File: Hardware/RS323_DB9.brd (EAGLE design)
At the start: 21.6 x 30.5 mm, 16 parts, among them U2 XN04312

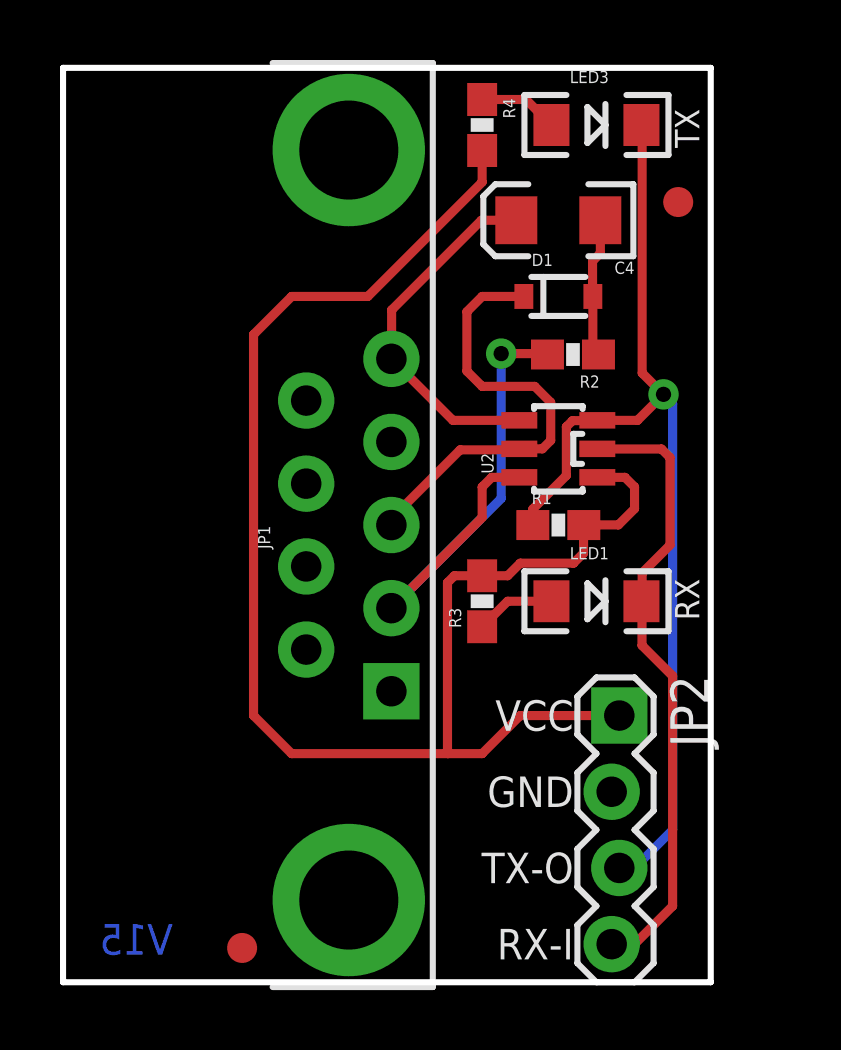
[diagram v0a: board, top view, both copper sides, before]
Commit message: Fixed headers, trace re route
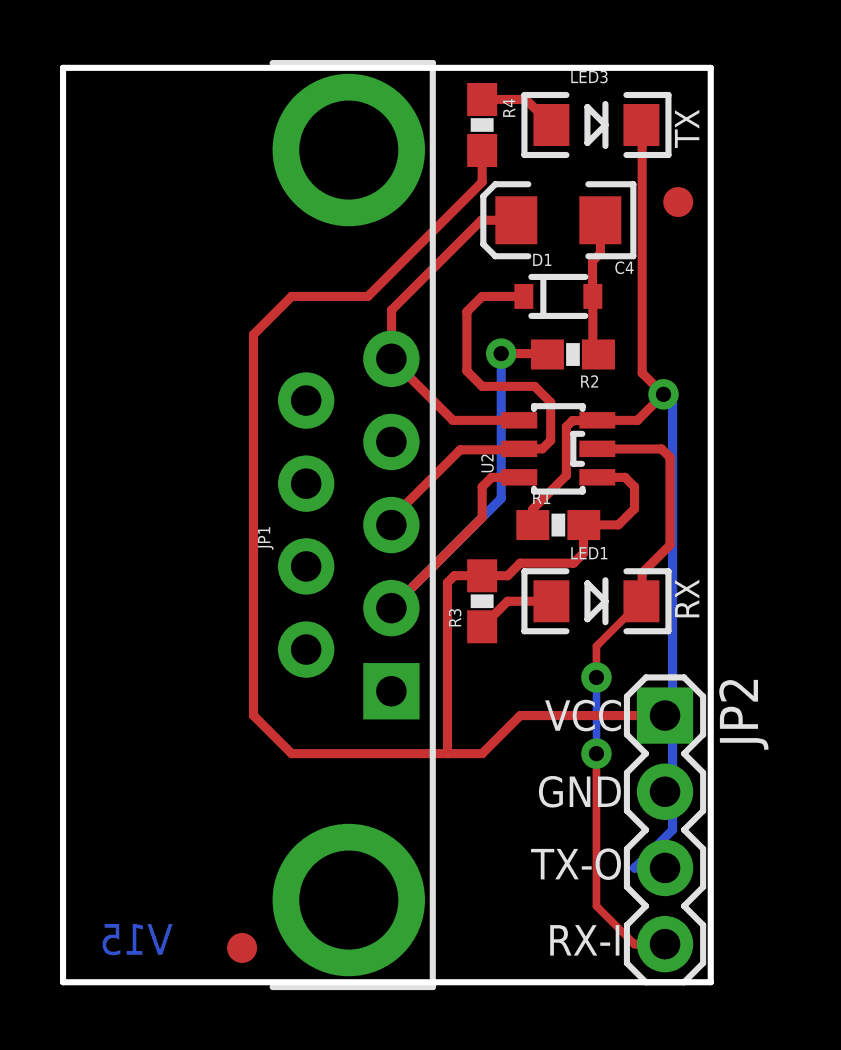
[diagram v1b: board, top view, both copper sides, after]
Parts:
- JP2: device SparkFun-Connectors:1X04_LOCK -> SparkFun-Connectors:1X04
- moved JP2 1.65 mm to (20.1, 8.89)
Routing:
- net VCC: track 52.7 -> 54.2 mm
- net TX: track 33.7 -> 34.2 mm
- net RX: track 21.1 -> 21.6 mm, vias 0 -> 2

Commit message: Fixed bad trace.
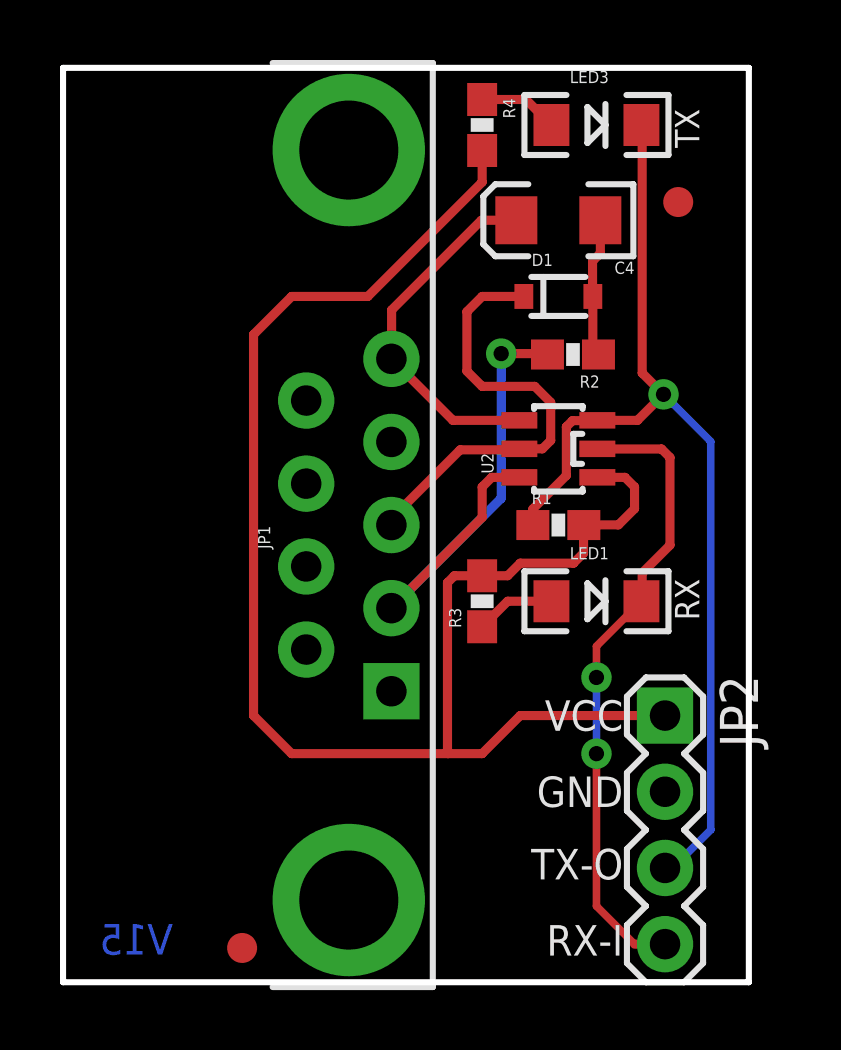
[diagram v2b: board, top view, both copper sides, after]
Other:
- board size 21.6 x 30.5 mm -> 22.9 x 30.5 mm
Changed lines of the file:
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@@
 <board>
 <plain>
-<wire x1="0" y1="0" x2="21.59" y2="0" width="0.2032" layer="20"/>
-<wire x1="21.59" y1="0" x2="21.59" y2="30.48" width="0.2032" layer="20"/>
-<wire x1="21.59" y1="30.48" x2="0" y2="30.48" width="0.2032" layer="20"/>
+<wire x1="0" y1="0" x2="22.86" y2="0" width="0.2032" layer="20"/>
+<wire x1="22.86" y1="0" x2="22.86" y2="30.48" width="0.2032" layer="20"/>
+<wire x1="22.86" y1="30.48" x2="0" y2="30.48" width="0.2032" layer="20"/>
 <wire x1="0" y1="30.48" x2="0" y2="0" width="0.2032" layer="20"/>
 <text x="18.669" y="1.905" size="1.016" layer="21" font="vector" ratio="15" rot="R180">RX-I</text>
@@
 <polygon width="0.2032" layer="16" isolate="0.3048">
 <vertex x="0" y="30.48"/>
-<vertex x="21.59" y="30.48"/>
-<vertex x="21.59" y="0"/>
+<vertex x="22.86" y="30.48"/>
+<vertex x="22.86" y="0"/>
 <vertex x="0" y="0"/>
 </polygon>
@@
 <wire x1="19.28" y1="28.472" x2="19.28" y2="28.575" width="0.3048" layer="1"/>
 <wire x1="19.304" y1="20.3073" x2="19.304" y2="28.448" width="0.3048" layer="1"/>
-<wire x1="20.066" y1="3.81" x2="19.05" y2="3.81" width="0.3048" layer="16"/>
-<wire x1="19.05" y1="3.81" x2="20.32" y2="5.08" width="0.3048" layer="16"/>
-<wire x1="20.32" y1="5.08" x2="20.32" y2="19.2913" width="0.3048" layer="16"/>
 <via x="20.0152" y="19.5961" extent="1-16" drill="0.508"/>
 <wire x1="20.32" y1="19.2913" x2="20.0152" y2="19.5961" width="0.3048" layer="16"/>
@@
 <wire x1="16.982440625" y1="18.7198" x2="17.7999" y2="18.7198" width="0.3048" layer="1"/>
 <wire x1="17.7999" y1="18.7198" x2="17.8101" y2="18.73" width="0.3048" layer="1"/>
+<wire x1="20.066" y1="3.81" x2="20.32" y2="3.81" width="0.254" layer="16"/>
+<wire x1="20.32" y1="3.81" x2="21.59" y2="5.08" width="0.254" layer="16"/>
+<wire x1="21.59" y1="5.08" x2="21.59" y2="18.0213" width="0.254" layer="16"/>
+<wire x1="21.59" y1="18.0213" x2="20.0152" y2="19.5961" width="0.254" layer="16"/>
 </signal>
 <signal name="N$4">

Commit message: fixed bad trace, added top ground plane.
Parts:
- FRAME1: value FRAME-LETTER -> (none)
- renumbered LED1 to D4, LED3 to D5
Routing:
- added copper zone on layer 1, net GND
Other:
- board text added: "N. Seidle"
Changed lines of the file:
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@@
 <layer number="27" name="tValues" color="7" fill="1" visible="no" active="yes"/>
 <layer number="28" name="bValues" color="7" fill="1" visible="no" active="yes"/>
-<layer number="29" name="tStop" color="7" fill="3" visible="no" active="yes"/>
+<layer number="29" name="tStop" color="7" fill="3" visible="yes" active="yes"/>
 <layer number="30" name="bStop" color="7" fill="6" visible="no" active="yes"/>
-<layer number="31" name="tCream" color="7" fill="4" visible="no" active="yes"/>
+<layer number="31" name="tCream" color="7" fill="4" visible="yes" active="yes"/>
 <layer number="32" name="bCream" color="7" fill="5" visible="no" active="yes"/>
 <layer number="33" name="tFinish" color="6" fill="3" visible="no" active="yes"/>
@@
 <layer number="39" name="tKeepout" color="4" fill="11" visible="no" active="yes"/>
 <layer number="40" name="bKeepout" color="1" fill="11" visible="no" active="yes"/>
-<layer number="41" name="tRestrict" color="4" fill="10" visible="no" active="yes"/>
+<layer number="41" name="tRestrict" color="4" fill="10" visible="yes" active="yes"/>
 <layer number="42" name="bRestrict" color="1" fill="10" visible="no" active="yes"/>
 <layer number="43" name="vRestrict" color="2" fill="10" visible="no" active="yes"/>
@@
 <layer number="45" name="Holes" color="7" fill="1" visible="yes" active="yes"/>
 <layer number="46" name="Milling" color="3" fill="1" visible="no" active="yes"/>
-<layer number="47" name="Measures" color="7" fill="1" visible="no" active="yes"/>
+<layer number="47" name="Measures" color="7" fill="1" visible="yes" active="yes"/>
 <layer number="48" name="Document" color="7" fill="1" visible="no" active="yes"/>
 <layer number="49" name="Reference" color="7" fill="1" visible="no" active="yes"/>
@@
 <text x="21.209" y="12.065" size="0.8128" layer="21" font="vector" ratio="15" rot="R90">RX</text>
 <text x="-5.08" y="-16.51" size="1.778" layer="51" font="vector" ratio="10">Revised by: Patrick Alberts</text>
+<dimension x1="0" y1="35.56" x2="22.86" y2="35.56" x3="11.43" y3="36.83" textsize="1.778" textratio="15" layer="47"/>
+<dimension x1="-13.97" y1="0" x2="-13.97" y2="30.48" x3="-15.24" y3="15.24" textsize="1.778" textratio="15" layer="47"/>
+<text x="13.335" y="-14.224" size="1.905" layer="51" font="vector" ratio="12">N. Seidle</text>
 </plain>
 <attributes>
@@
 <attribute name="VALUE" x="6.11" y="14.55" size="0.4064" layer="27" ratio="10" rot="R90"/>
 </element>
-<element name="LED1" library="SparkFun" package="LED-1206" value="Red" x="17.78" y="12.7" smashed="yes">
+<element name="D4" library="SparkFun" package="LED-1206" value="Red" x="17.78" y="12.7" smashed="yes">
 <attribute name="NAME" x="16.891" y="14.097" size="0.4064" layer="25"/>
 <attribute name="VALUE" x="17.272" y="11.303" size="0.4064" layer="27"/>
 </element>
-<element name="LED3" library="SparkFun" package="LED-1206" value="Grn" x="17.78" y="28.575" smashed="yes">
+<element name="D5" library="SparkFun" package="LED-1206" value="Grn" x="17.78" y="28.575" smashed="yes">
 <attribute name="NAME" x="16.891" y="29.972" size="0.4064" layer="25"/>
 <attribute name="VALUE" x="17.399" y="27.432" size="0.4064" layer="27"/>
@@
 <element name="E$1" library="SparkFun" package="FIDUCIAL-1X2" value="FIDUCIAL1X2" x="5.969" y="1.143"/>
 <element name="E$2" library="SparkFun" package="FIDUCIAL-1X2" value="FIDUCIAL1X2" x="20.50541875" y="26.007059375"/>
-<element name="FRAME1" library="SparkFun-Aesthetics" package="CREATIVE_COMMONS" value="FRAME-LETTER" x="-16.69305625" y="-13.97"/>
+<element name="FRAME1" library="SparkFun-Aesthetics" package="CREATIVE_COMMONS" value="" x="-16.69305625" y="-13.97" smashed="yes">
+<attribute name="VERSION" value="v01" x="12.51694375" y="-3.81" size="1.27" layer="16" font="vector" ratio="15" rot="SMR0" display="off"/>
+<attribute name="DESIGNER" value="NAME" x="9.97694375" y="-13.97" size="1.778" layer="51" display="off"/>
+</element>
 <element name="LOGO2" library="SparkFun-Aesthetics" package="OSHW-LOGO-M" value="OSHW-LOGOM" x="2.98958125" y="27.3685" rot="MR270"/>
 <element name="LOGO1" library="SparkFun-Aesthetics" package="SFE_LOGO_NAME_FLAME_.1" value="SFE_LOGO_NAME_FLAME.1_INCH" x="6.131559375" y="21.10739375" rot="MR270"/>
@@
 <wire x1="12.995" y1="18.73" x2="10.95248125" y2="20.77251875" width="0.3048" layer="1"/>
 <wire x1="10.95248125" y1="20.77251875" x2="10.945" y2="20.78" width="0.3048" layer="1"/>
+<polygon width="0.3048" layer="1" isolate="0.3048">
+<vertex x="0" y="0"/>
+<vertex x="0" y="30.48"/>
+<vertex x="22.86" y="30.48"/>
+<vertex x="22.86" y="0"/>
+</polygon>
 </signal>
 <signal name="VCC">
@@
 </signal>
 <signal name="N$1">
-<contactref element="LED1" pad="A"/>
+<contactref element="D4" pad="A"/>
 <contactref element="R3" pad="1"/>
 <wire x1="16.28" y1="12.7" x2="16.51" y2="12.7" width="0.3048" layer="1"/>
@@
 </signal>
 <signal name="N$2">
-<contactref element="LED3" pad="A"/>
+<contactref element="D5" pad="A"/>
 <contactref element="R4" pad="1"/>
 <wire x1="16.256" y1="28.575" x2="16.28" y2="28.575" width="0.3048" layer="1"/>
@@
 </signal>
 <signal name="RX">
-<contactref element="LED1" pad="C"/>
+<contactref element="D4" pad="C"/>
 <contactref element="JP2" pad="4"/>
 <contactref element="U2" pad="2"/>
@@
 </signal>
 <signal name="TX">
-<contactref element="LED3" pad="C"/>
+<contactref element="D5" pad="C"/>
 <contactref element="R1" pad="1"/>
 <contactref element="JP2" pad="3"/>
